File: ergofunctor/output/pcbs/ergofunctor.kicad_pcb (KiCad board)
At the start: 2 copper layers, 155.9 x 135.1 mm, 56 parts

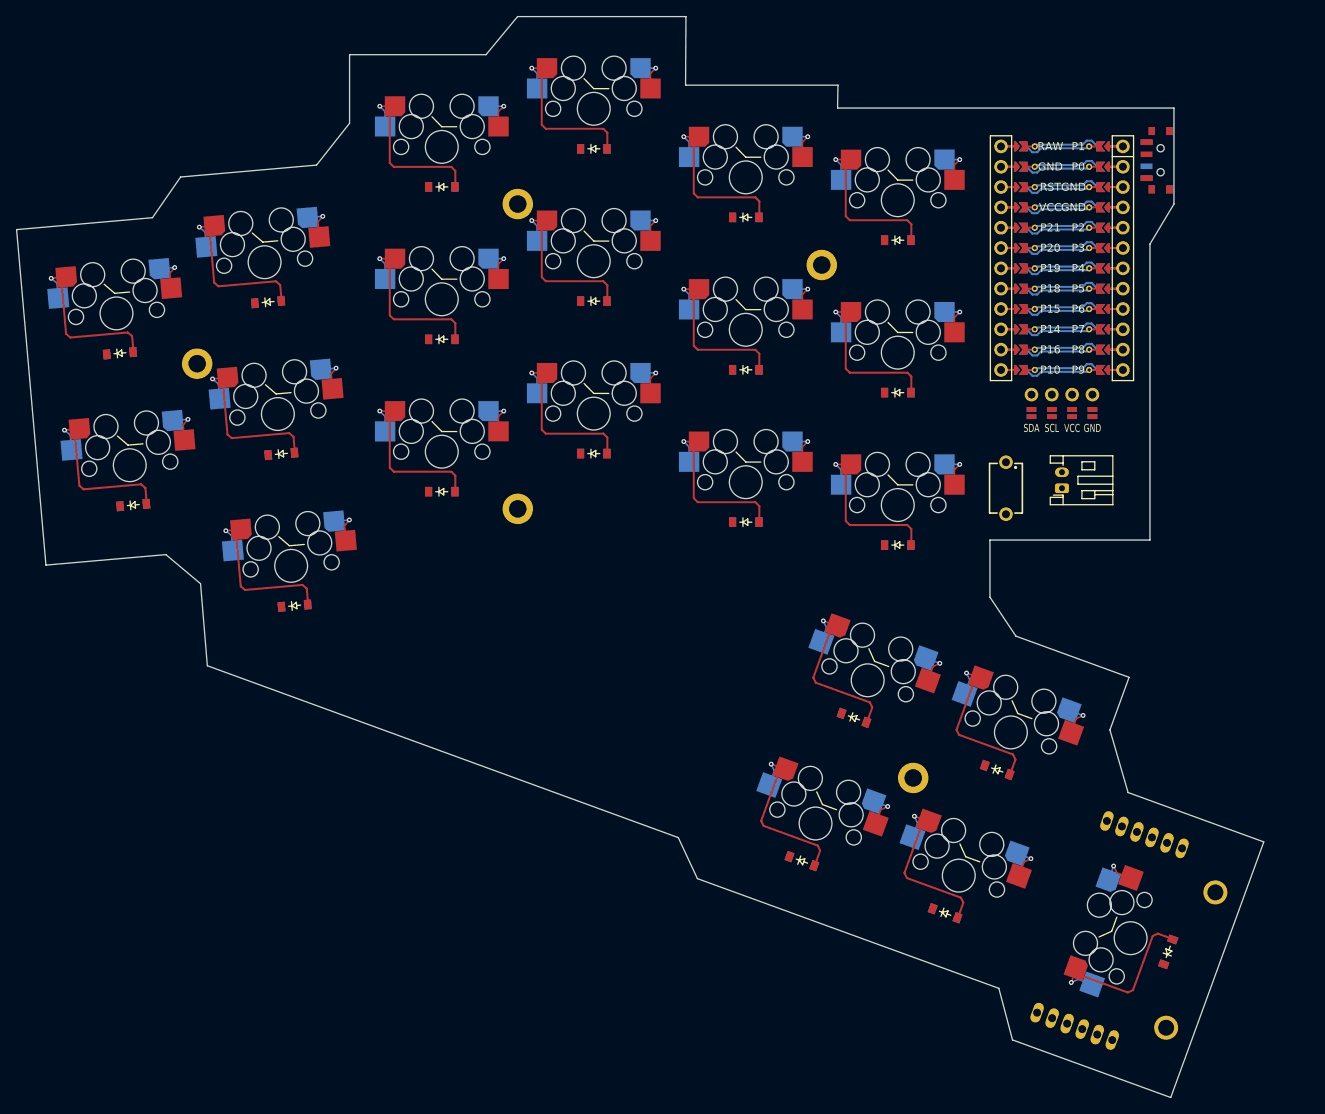
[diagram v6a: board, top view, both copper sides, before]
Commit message: fix path to diode
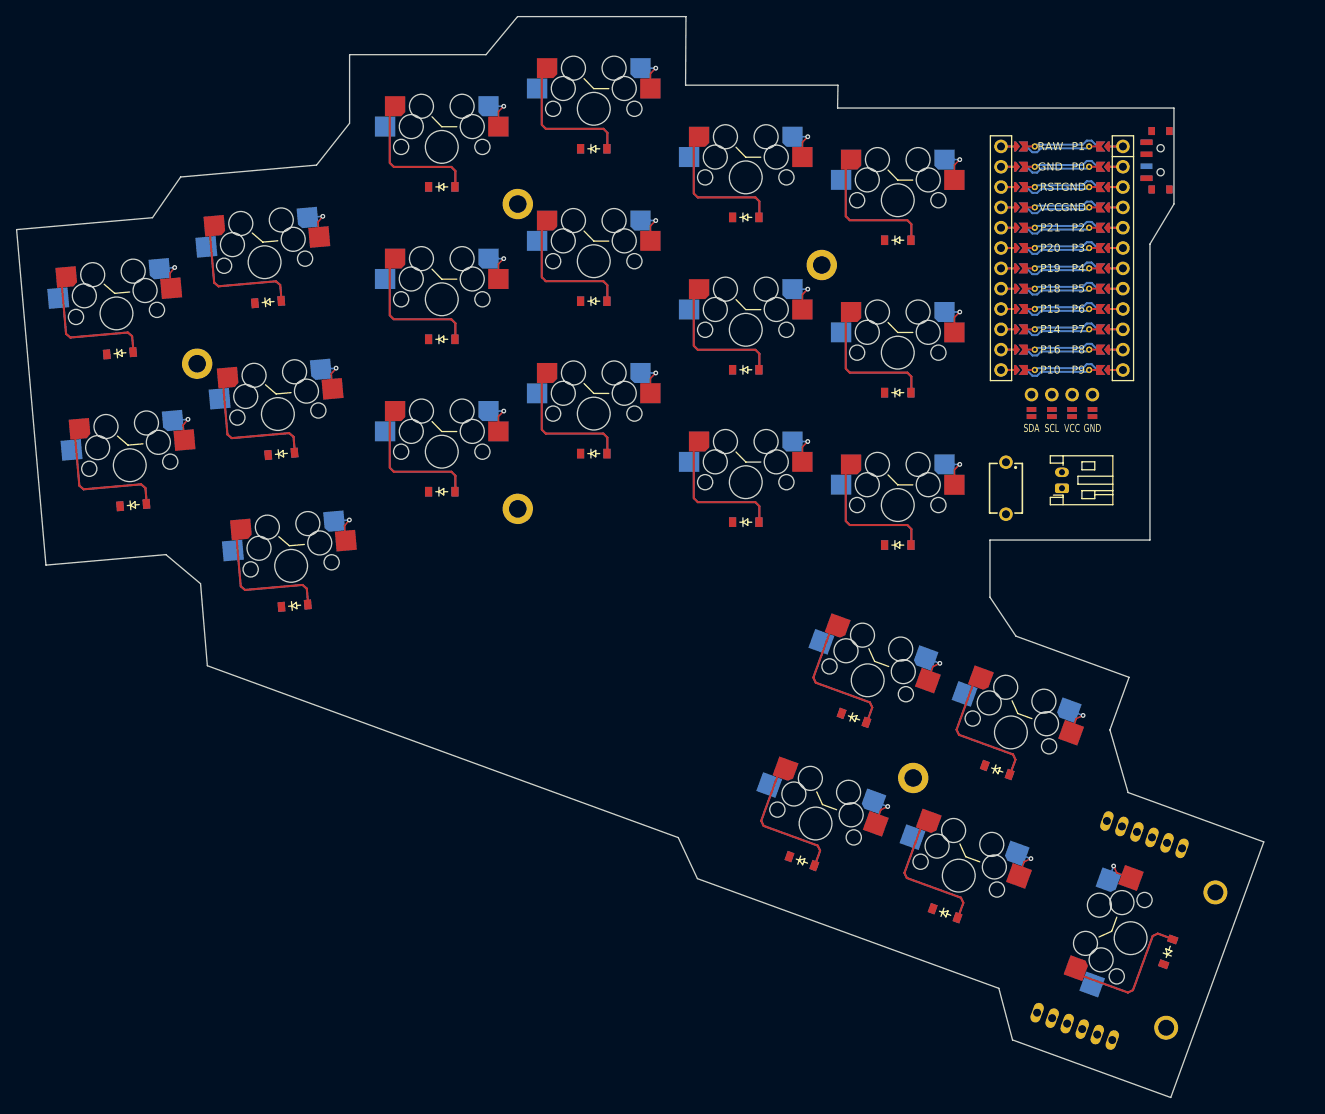
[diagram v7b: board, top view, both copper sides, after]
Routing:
- net middle_top_row: track 22.6 -> 32.5 mm, vias 1 -> 0
- net outer_bottom_row: track 22.6 -> 32.5 mm, vias 1 -> 0
- net inner_bottom: track 22.6 -> 32.5 mm, vias 1 -> 0
- net middle_bottom: track 22.6 -> 32.5 mm, vias 1 -> 0
- net inner_top: track 22.6 -> 32.5 mm, vias 1 -> 0
- net inner_home: track 22.6 -> 32.5 mm, vias 1 -> 0
- net ring_top: track 22.6 -> 32.5 mm, vias 1 -> 0
- net middle_home: track 22.6 -> 32.5 mm, vias 1 -> 0
- net index_top: track 22.6 -> 32.5 mm, vias 1 -> 0
- net index_home: track 22.6 -> 32.5 mm, vias 1 -> 0
- net ring_bottom: track 22.6 -> 32.5 mm, vias 1 -> 0
- net index_bottom: track 22.6 -> 32.5 mm, vias 1 -> 0
- net ring_home: track 22.6 -> 32.5 mm, vias 1 -> 0
- net middle_top: track 22.6 -> 32.5 mm, vias 1 -> 0
- net outer_top: track 22.6 -> 32.5 mm, vias 1 -> 0
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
